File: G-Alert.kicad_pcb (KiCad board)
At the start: 2 copper layers, 39.1 x 91.4 mm, 19 parts, among them SW1 SW_Push, U1 MQ-4b, U2 LM393

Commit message: pcb-semifinal
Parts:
- moved D3 140.2 mm to (25.4, 90.0)
- moved R2 135.5 mm to (30.5, 107.3)
- moved R6 135.5 mm to (29.5, 51.9), turned to -90 degrees
- moved D4 125.1 mm to (37.8, 108.3), turned to 0 degrees
- moved R1 118.6 mm to (31.5, 23.5)
- moved D2 118.2 mm to (48.1, 77.4)
- moved D5 118.2 mm to (35.6, 77.3)
- moved SW1 118.2 mm to (39.5, 97.7)
- moved U3 118.2 mm to (41.9, 22.4)
- moved U1 118.2 mm to (38.5, 37.4)
- moved BZ1 118.2 mm to (45.7, 61.1)
- moved R_Var1 116.7 mm to (51.4, 56.5), turned to 0 degrees
- moved D1 111.5 mm to (45.5, 102.7), turned to 180 degrees
- moved R7 101.1 mm to (47.2, 70.7), turned to 180 degrees
- moved R5 99.1 mm to (52.3, 81.9), turned to -90 degrees
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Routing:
- net Net-(U1-B1): track 40.0 -> 61.5 mm
- net Net-(C1-Pad1): track 63.8 -> 43.5 mm
- net +5V: track 142.3 -> 123.8 mm
- net Net-(U2A--): track 32.9 -> 17.0 mm
- net Net-(D2-A): track 9.08 -> 22.9 mm
- net Net-(D3-G): track 33.8 -> 26.7 mm
- net Net-(BZ1--): track 64.5 -> 58.5 mm
- net Net-(D1-K): track 13.6 -> 14.3 mm
- added copper zone on F.Cu, net GND
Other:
- board size 39.1 x 91.4 mm -> 42.2 x 93.5 mm

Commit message: Panel Update
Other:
- board text added: "Bivob.BD"
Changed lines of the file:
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@@
 		(capping no)
 		(filling no)
-		(zone_defaults)
 		(pcbplotparams
 			(layerselection 0x00000000_00000000_55555555_5755f5ff)
@@
 		(layer "Edge.Cuts")
 	)
+	(gr_text "Bivob.BD"
+		(at 60.75 41.75 90)
+		(layer "F.SilkS")
+		(effects
+			(font
+				(size 2 2)
+			)
+			(justify left bottom)
+		)
+	)
 	(segment
 		(start 52.324 72.268)
@@
 	)
 	(segment
-		(start 38.491 37.375)
-		(end 39.491 38.375)
-		(width 0.6)
-		(layer "F.Cu")
-		(net "Net-(U1-B1)")
-	)
-	(segment
-		(start 39.491 38.375)
-		(end 39.491 43.095)
-		(width 0.6)
-		(layer "F.Cu")
-		(net "Net-(U1-B1)")
-	)
-	(segment
 		(start 54.864 62.103)
 		(end 53.848 61.087)
@@
 	)
 	(segment
-		(start 39.491 43.095)
-		(end 38.491 44.095)
+		(start 54.864 64.897)
+		(end 54.864 62.103)
 		(width 0.6)
 		(layer "F.Cu")
@@
 	)
 	(segment
-		(start 54.864 64.897)
-		(end 54.864 62.103)
+		(start 40 38.884)
+		(end 40 42.586)
 		(width 0.6)
 		(layer "F.Cu")
@@
 	)
 	(segment
+		(start 38.491 37.375)
+		(end 40 38.884)
+		(width 0.6)
+		(layer "F.Cu")
+		(net "Net-(U1-B1)")
+	)
+	(segment
 		(start 35.052 33.655)
 		(end 38.491 37.094)
 		(width 0.6)
 		(layer "F.Cu")
+		(net "Net-(U1-B1)")
+	)
+	(segment
+		(start 40 42.586)
+		(end 38.491 44.095)
+		(width 0.6)
+		(layer "F.Cu")

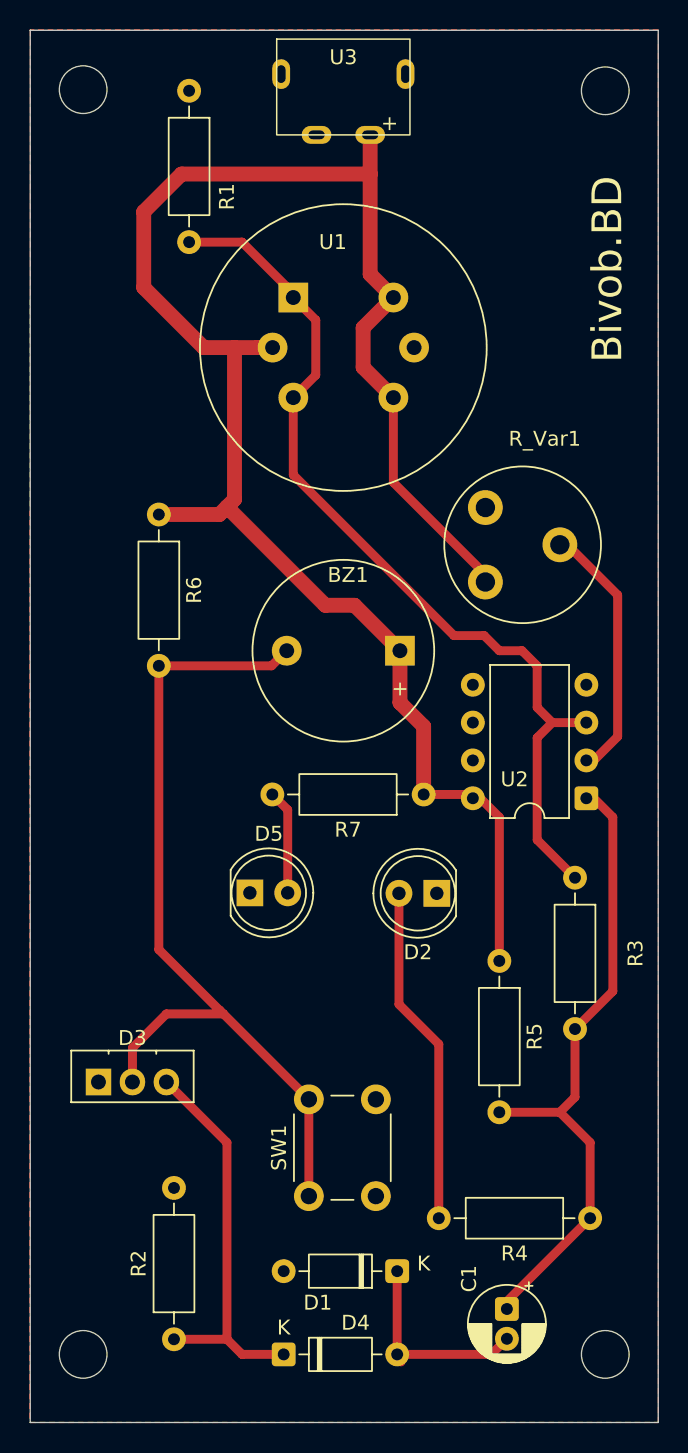
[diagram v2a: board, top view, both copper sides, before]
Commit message: Single Side Correction Update
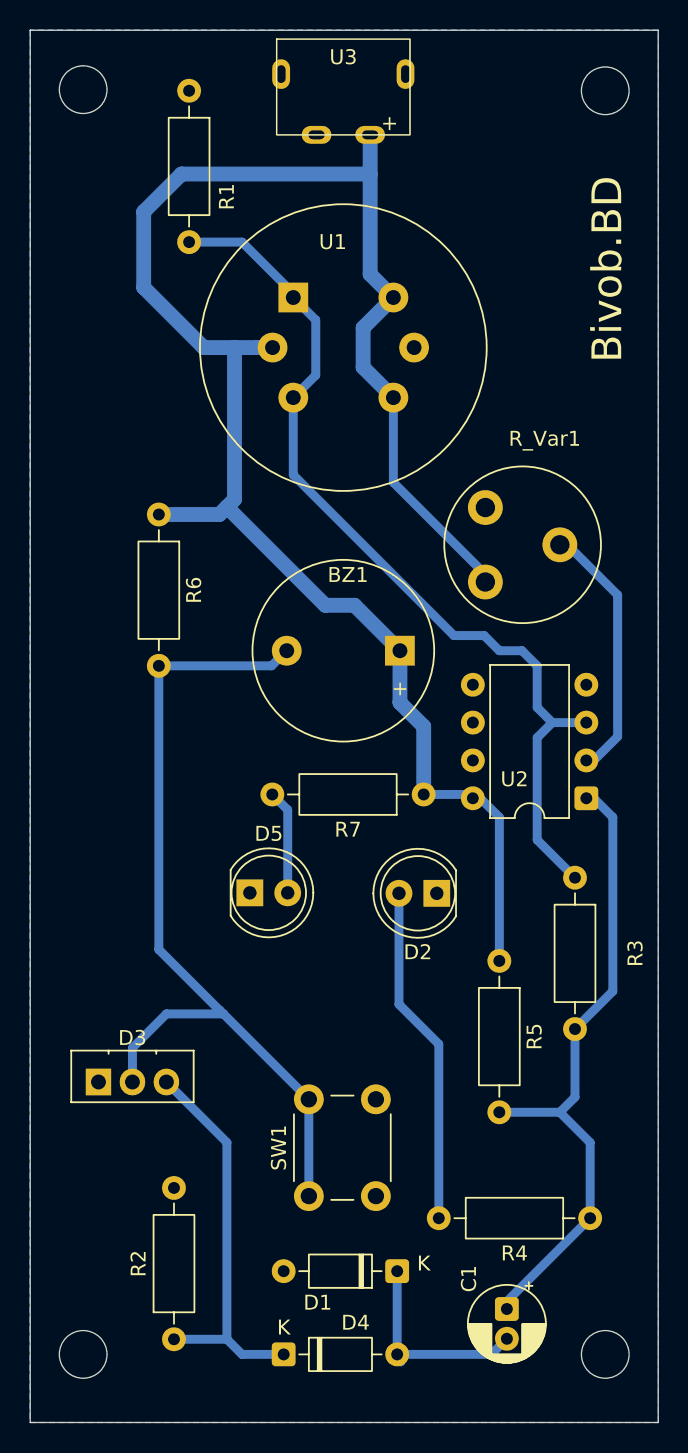
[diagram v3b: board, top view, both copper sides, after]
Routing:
- added copper zone on B.Cu, net GND
- removed copper zone on F.Cu, net GND
